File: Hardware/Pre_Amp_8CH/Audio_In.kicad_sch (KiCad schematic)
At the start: 0 parts

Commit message: RCA in & OUT
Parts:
- added J1: PJRAS4X2U01AUX, Pre_Amp_8CH_Footprints:PJRAS4X2U01AUX, symbol Pre_Amp_8CH_Symbols:PJRAS4X2U01AUX
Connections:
- new net GNDA: J1.S1, J1.S2, J1.S3, J1.S4
- new net IN1L: J1.T11
- new net IN1R: J1.T12
- new net IN2L: J1.T21
- new net IN2R: J1.T22
- new net IN3L: J1.T31
- new net IN3R: J1.T32
- new net IN4L: J1.T41
- new net IN4R: J1.T42

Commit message: DSP start
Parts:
- renumbered J1 to J301
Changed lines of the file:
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@@
 		(dnp no)
 		(fields_autoplaced yes)
-		(property "Reference" "#PWR01"
+		(property "Reference" "#PWR0301"
 			(at 50.8 64.77 0)
 			(effects
@@
 			(project "Pre_Amp_8CH"
 				(path "/95391f5e-c27a-414f-9293-205fef445dea/6f33af91-558f-4906-ad66-170a43f0e6d3"
-					(reference "#PWR01")
+					(reference "#PWR0301")
 					(unit 1)
 				)
@@
 		(on_board yes)
 		(dnp no)
-		(property "Reference" "J1"
+		(property "Reference" "J301"
 			(at 39.37 35.052 0)
 			(effects
@@
 			(project "Pre_Amp_8CH"
 				(path "/95391f5e-c27a-414f-9293-205fef445dea/6f33af91-558f-4906-ad66-170a43f0e6d3"
-					(reference "J1")
+					(reference "J301")
 					(unit 1)
 				)
@@
 		(dnp no)
 		(fields_autoplaced yes)
-		(property "Reference" "#PWR02"
+		(property "Reference" "#PWR0302"
 			(at 76.2 64.77 0)
 			(effects
@@
 			(project "Pre_Amp_8CH"
 				(path "/95391f5e-c27a-414f-9293-205fef445dea/6f33af91-558f-4906-ad66-170a43f0e6d3"
-					(reference "#PWR02")
+					(reference "#PWR0302")
 					(unit 1)
 				)
@@
 		(dnp no)
 		(fields_autoplaced yes)
-		(property "Reference" "#PWR04"
+		(property "Reference" "#PWR0304"
 			(at 127 64.77 0)
 			(effects
@@
 			(project "Pre_Amp_8CH"
 				(path "/95391f5e-c27a-414f-9293-205fef445dea/6f33af91-558f-4906-ad66-170a43f0e6d3"
-					(reference "#PWR04")
+					(reference "#PWR0304")
 					(unit 1)
 				)
@@
 		(dnp no)
 		(fields_autoplaced yes)
-		(property "Reference" "#PWR03"
+		(property "Reference" "#PWR0303"
 			(at 101.6 64.77 0)
 			(effects
@@
 			(project "Pre_Amp_8CH"
 				(path "/95391f5e-c27a-414f-9293-205fef445dea/6f33af91-558f-4906-ad66-170a43f0e6d3"
-					(reference "#PWR03")
-					(unit 1)
-				)
+					(reference "#PWR0303")
+					(unit 1)
+				)

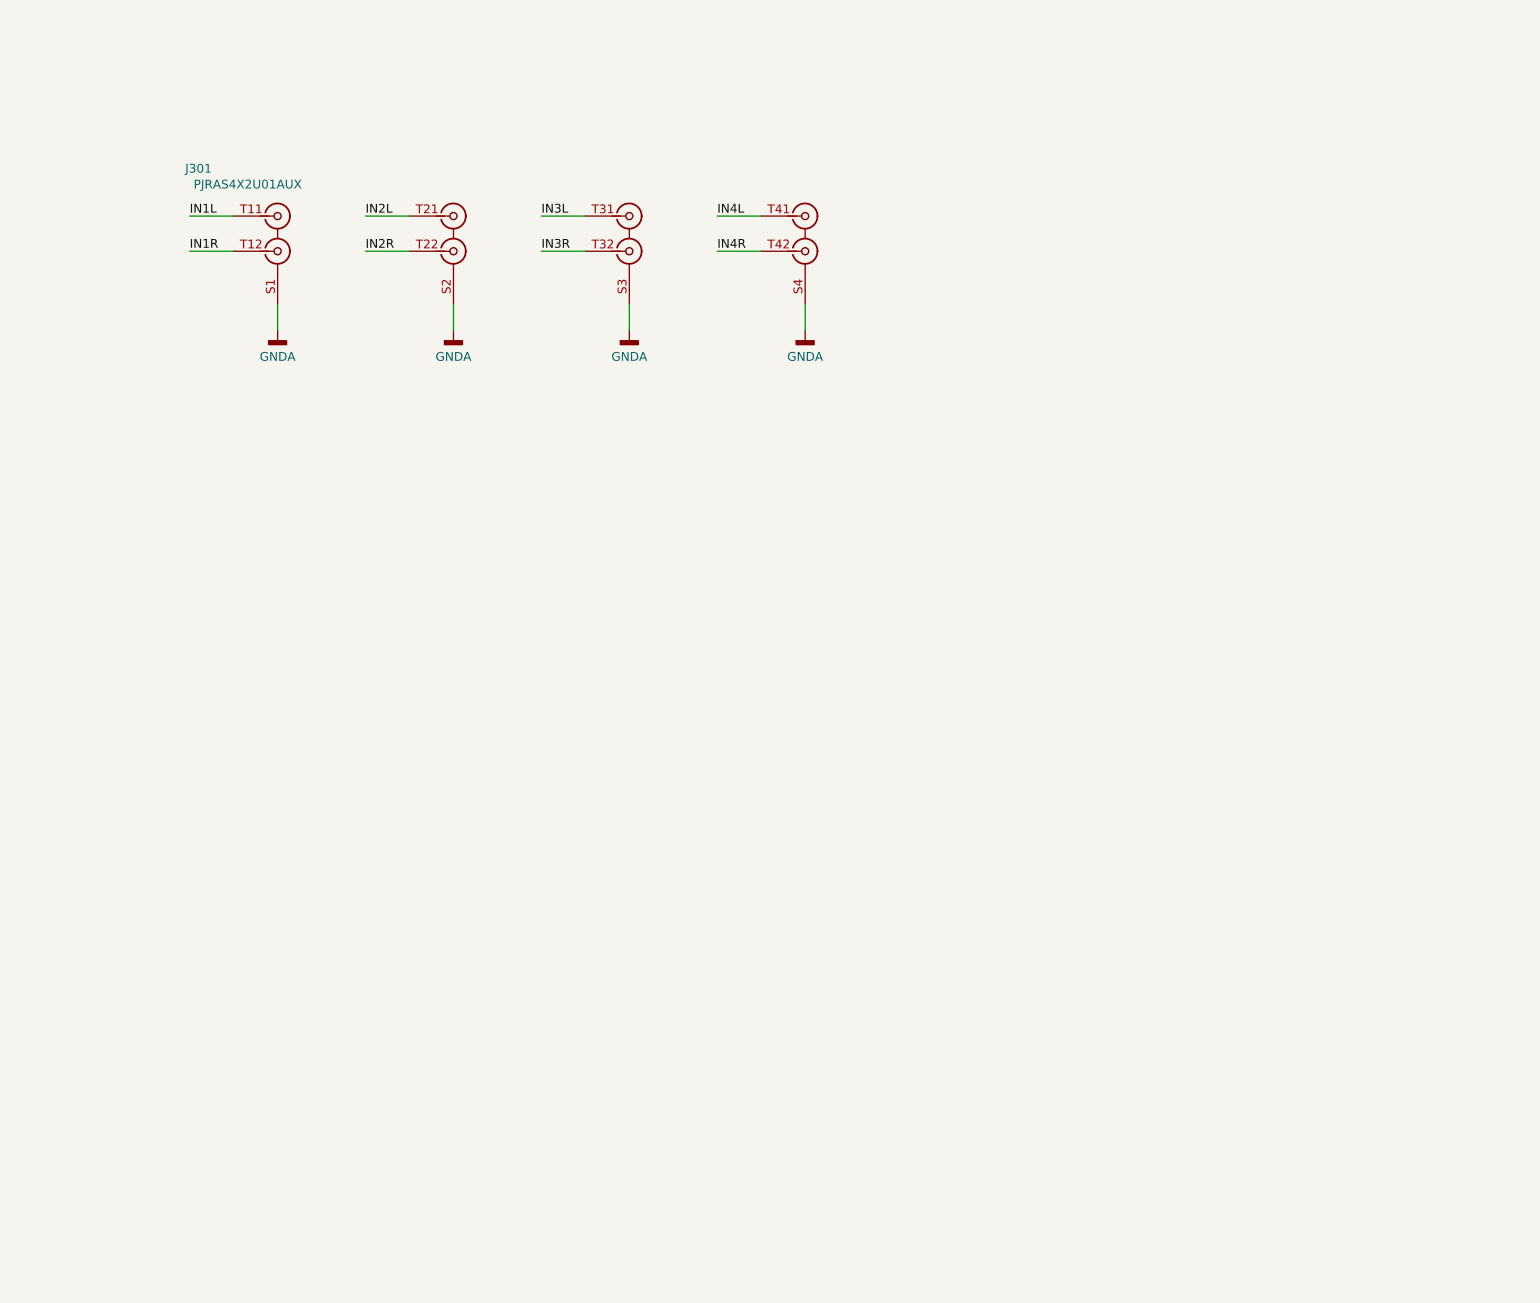
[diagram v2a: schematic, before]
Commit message: audio input buffers
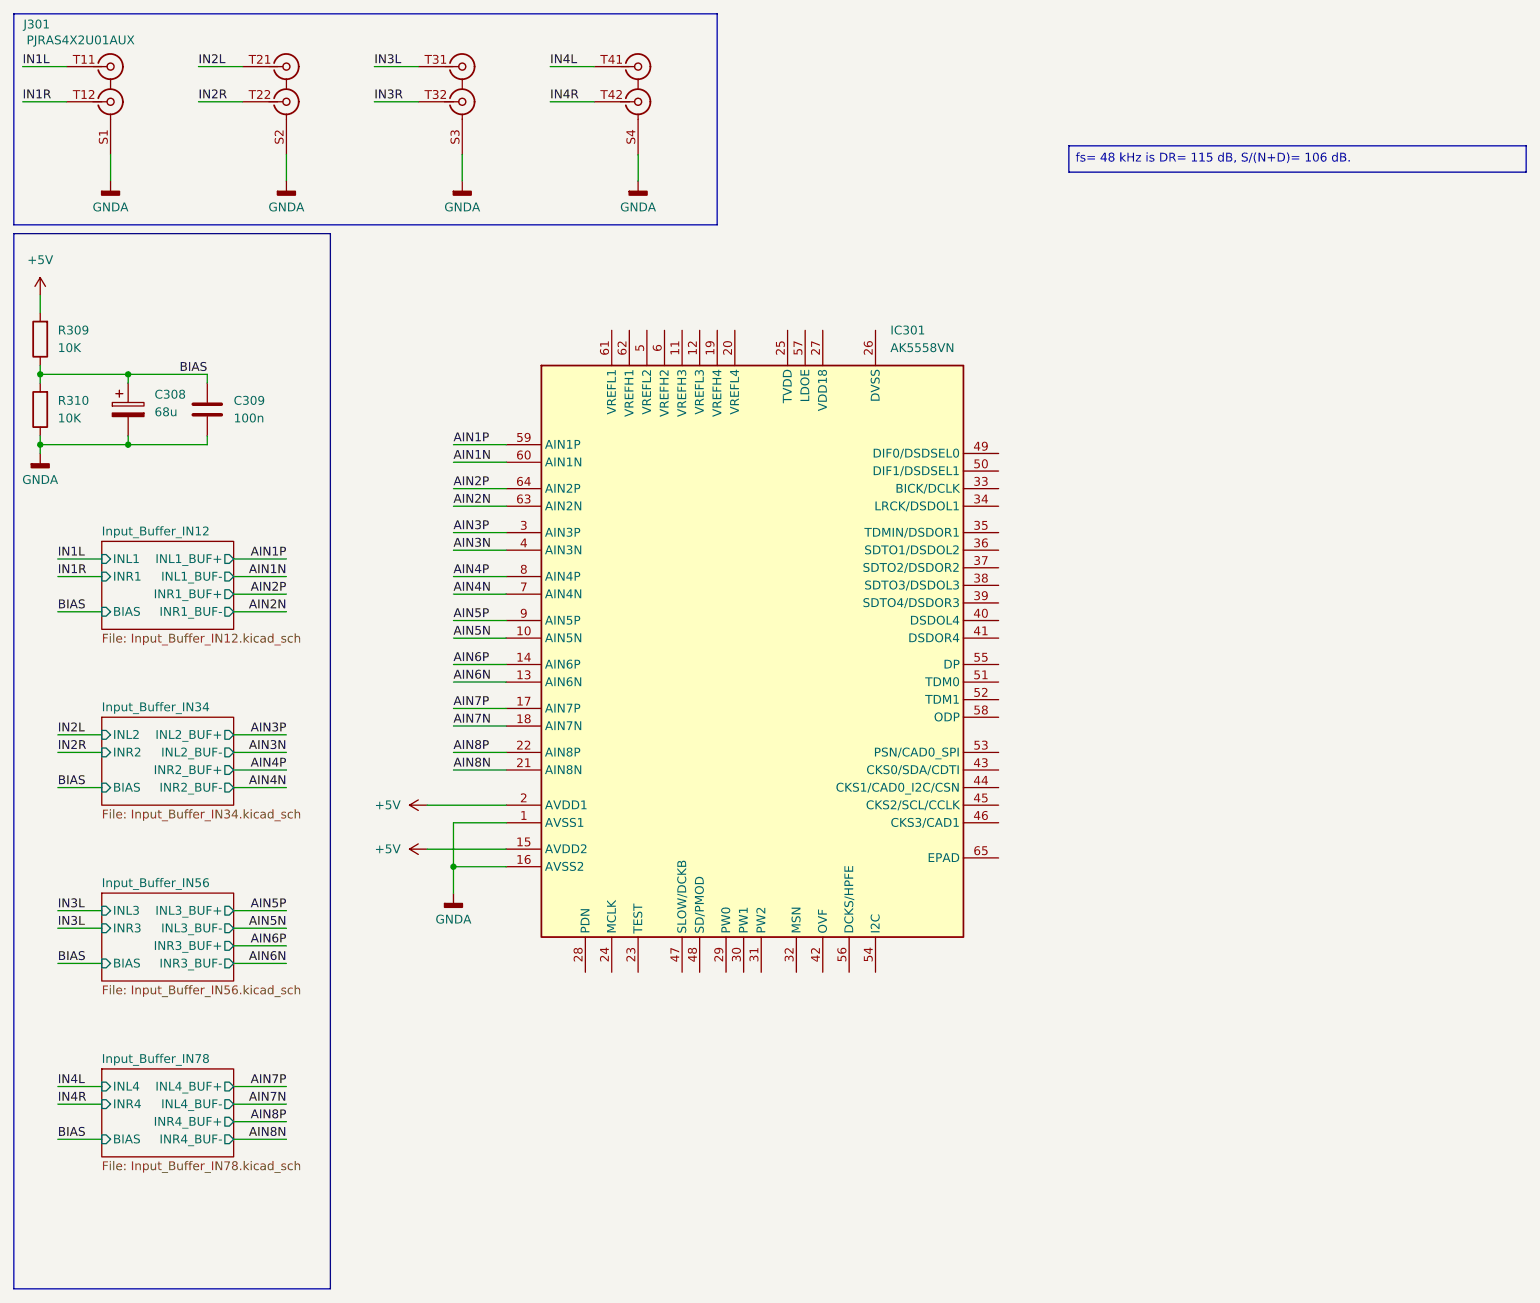
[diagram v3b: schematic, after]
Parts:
- added C308: 68u, symbol Device:C_Polarized
- added C309: 100n, Capacitor_SMD:C_0603_1608Metric_Pad1.08x0.95mm_HandSolder, symbol Device:C
- added IC301: AK5558VN, Pre_Amp_8CH_Footprints:QFN50P900X900X100-65N, symbol Pre_Amp_8CH_Symbols:AK5558VN
- added R309, R310: 10K, Resistor_SMD:R_0603_1608Metric_Pad0.98x0.95mm_HandSolder, symbol Device:R
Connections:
- net GNDA: now also C308.2, C309.2, IC301.1 (AVSS1), IC301.16 (AVSS2), R310.1
- new net +5V: IC301.15 (AVDD2), IC301.2 (AVDD1), R309.2
- new net AIN1N: IC301.60 (AIN1N)
- new net AIN1P: IC301.59 (AIN1P)
- new net AIN2N: IC301.63 (AIN2N)
- new net AIN2P: IC301.64 (AIN2P)
- new net AIN3N: IC301.4 (AIN3N)
- new net AIN3P: IC301.3 (AIN3P)
- new net AIN4N: IC301.7 (AIN4N)
- new net AIN4P: IC301.8 (AIN4P)
- new net AIN5N: IC301.10 (AIN5N)
- new net AIN5P: IC301.9 (AIN5P)
- new net AIN6N: IC301.13 (AIN6N)
- new net AIN6P: IC301.14 (AIN6P)
- new net AIN7N: IC301.18 (AIN7N)
- new net AIN7P: IC301.17 (AIN7P)
- new net AIN8N: IC301.21 (AIN8N)
- new net AIN8P: IC301.22 (AIN8P)
- new net BIAS: C308.1, C309.1, R309.1, R310.2
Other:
- added sheet Input_Buffer_IN12 (Input_Buffer_IN12.kicad_sch)
- added sheet Input_Buffer_IN34 (Input_Buffer_IN34.kicad_sch)
- added sheet Input_Buffer_IN56 (Input_Buffer_IN56.kicad_sch)
- added sheet Input_Buffer_IN78 (Input_Buffer_IN78.kicad_sch)
- moved on the sheet: J301
